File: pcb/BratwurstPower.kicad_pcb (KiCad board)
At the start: 4 copper layers, 85 x 56 mm, 130 parts, among them J1 BarrelJack, J10 GPIO, J2 Raspi, J3 USB1in, J4 USB1out, J5 I2C, J6 I2C, J7 USB2in, J8 USB2out, J9 EXT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

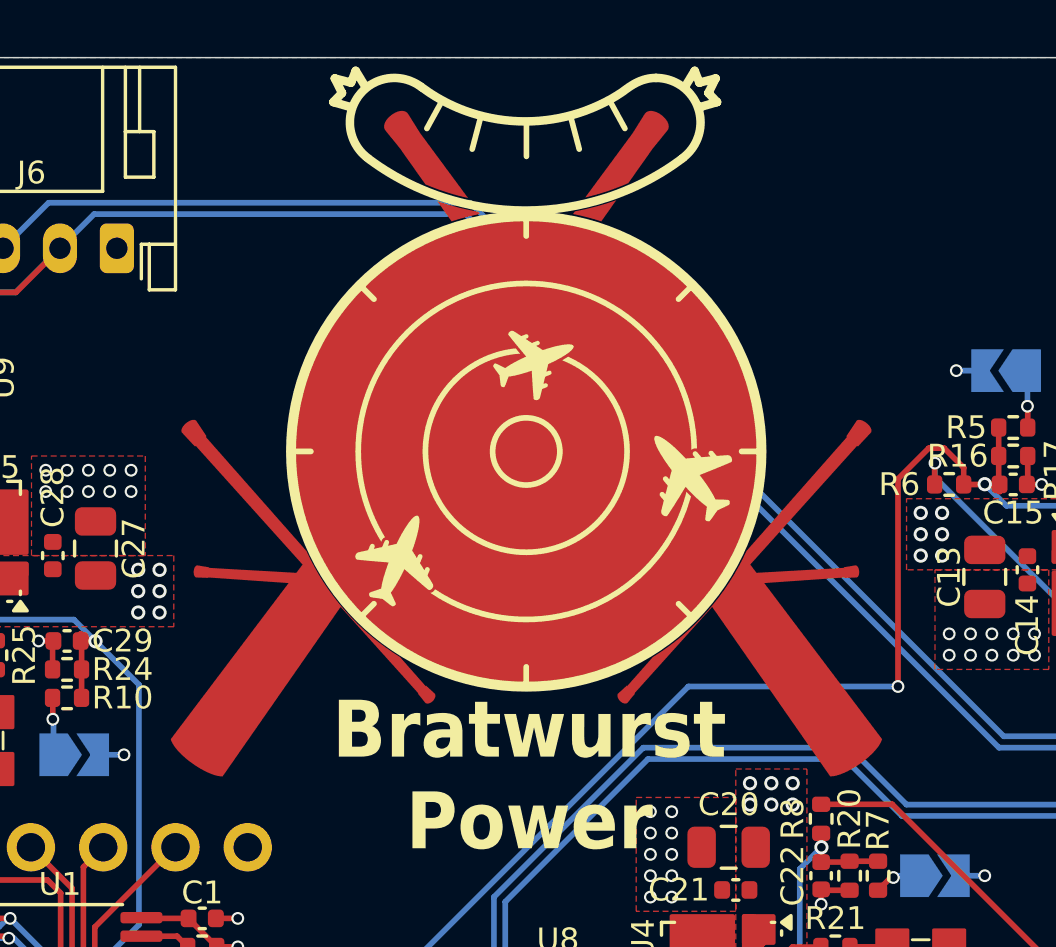
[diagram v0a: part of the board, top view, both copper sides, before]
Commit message: fix: update Bratwurst Logo
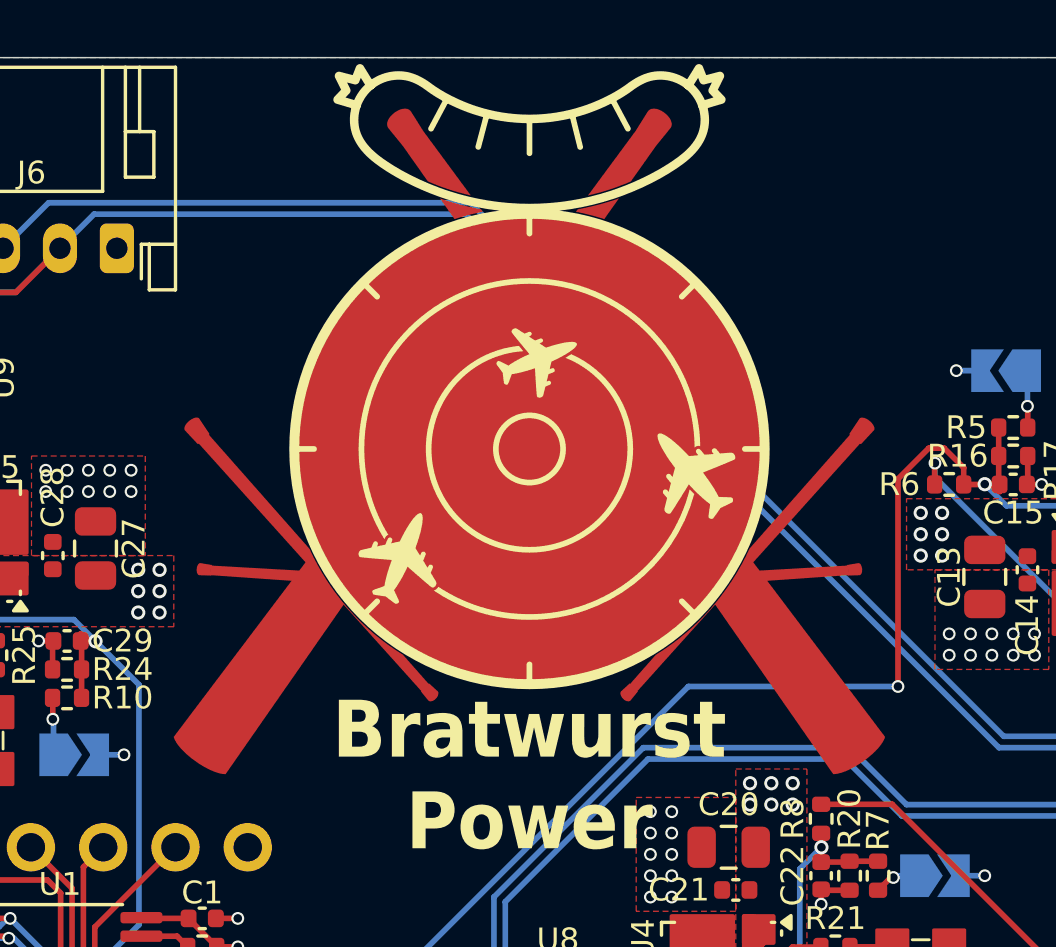
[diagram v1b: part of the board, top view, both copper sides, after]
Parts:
- removed the REF** at (168.2, 92.8)
- added REF**: BratwurstLogo_Filled, BratwurstPower:BratwurstLogo_Filled, F.Cu at (168.2, 93.8)

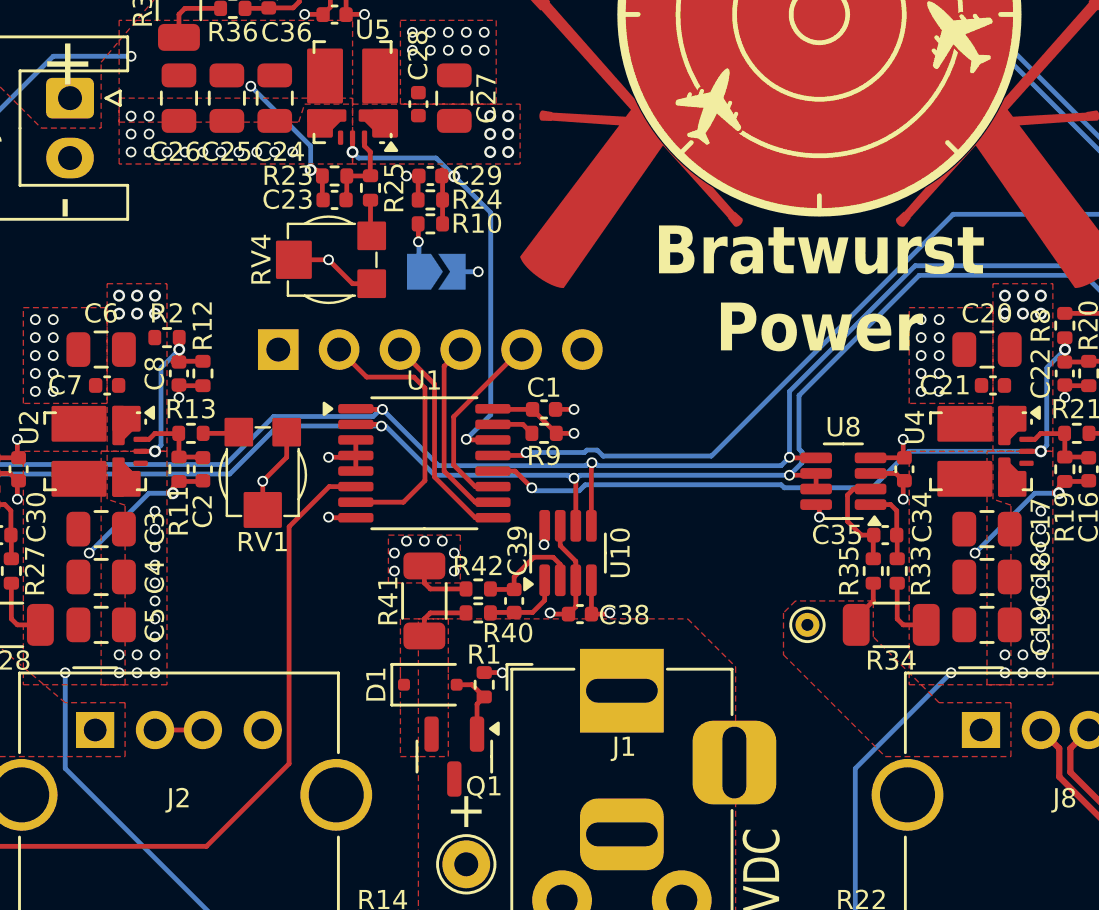
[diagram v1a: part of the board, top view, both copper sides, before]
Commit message: feat: add optional input cap
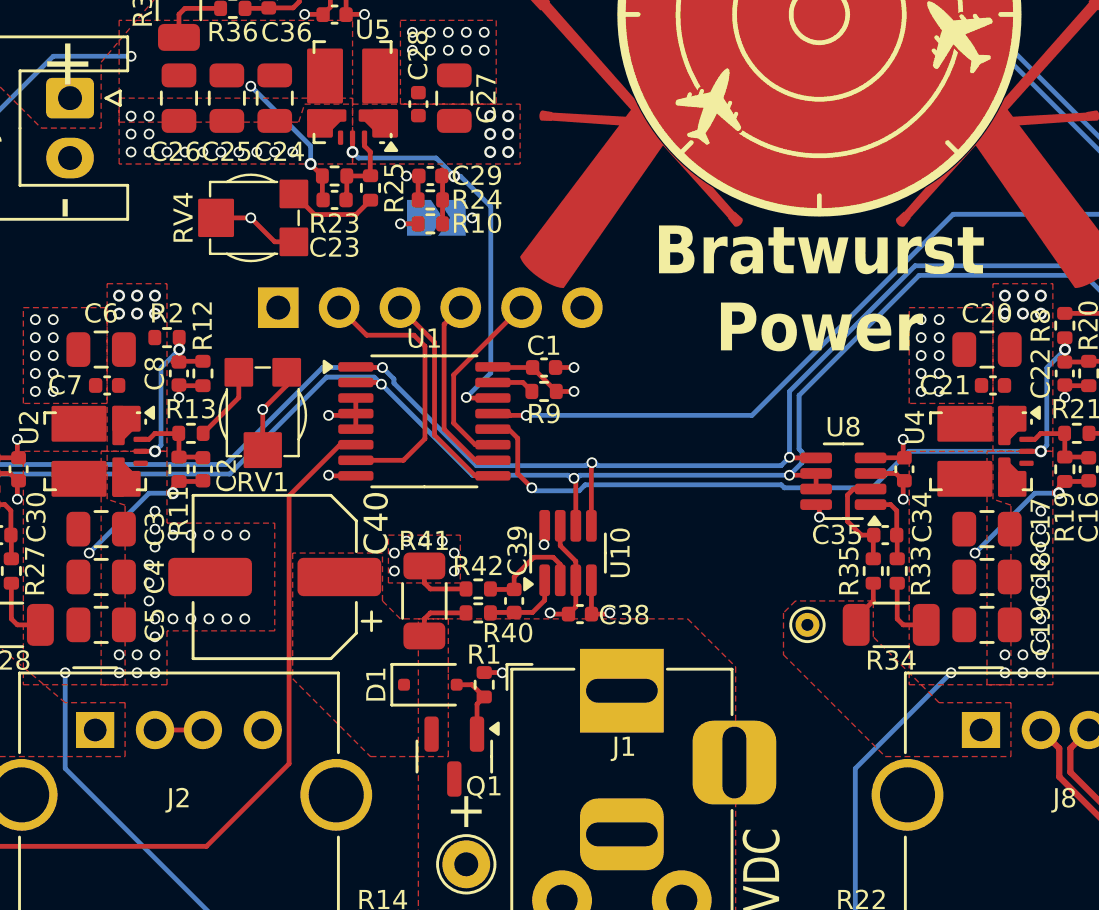
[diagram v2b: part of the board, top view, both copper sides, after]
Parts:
- added C40: 100uF, Capacitor_SMD:CP_Elec_6.3x5.8, F.Cu at (145.5, 117.2)
- moved RV4 3.69 mm to (144.5, 102.2)
- moved RV1 2.50 mm to (145.0, 110.5)
- moved JP3 2.25 mm to (152.2, 102.2)
- moved C1 1.75 mm to (156.8, 108.5)
- moved J10 1.75 mm to (145.7, 106.0)
- moved R9 1.75 mm to (156.8, 109.5)
- moved U1 1.75 mm to (151.8, 110.8)
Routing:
- net /BuckEXT/FBt: track 1.51 -> 3.88 mm
- net SDA: track 140.3 -> 142.0 mm
- net /BuckRaspi/FBt: track 1.51 -> 3.17 mm
- net /Een: track 21.1 -> 19.5 mm
- net /U2en: track 32.3 -> 33.9 mm
- net SCL: track 140.7 -> 142.3 mm
- net /~{BLen}: track 29.4 -> 30.9 mm
- net /U1en: track 50.6 -> 49.7 mm
- net GND: vias 120 -> 130

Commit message: chore: one shall save before committing
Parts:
- C40: footprint Capacitor_SMD:CP_Elec_6.3x5.8 -> Capacitor_THT:CP_Radial_D6.3mm_P2.50mm
- moved C40 1.75 mm to (147.2, 117.2)
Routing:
- net GND: vias 130 -> 120

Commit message: fix: I2C pull-up strength
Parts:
- R3, R4: value 3k3 -> 2k2
- moved JP2 11.9 mm to (180.5, 120.5), turned to 180 degrees
- moved JP1 9.66 mm to (194.5, 92.8), turned to 0 degrees
- moved J10 3.75 mm to (149.4, 106.0)
- moved JP3 2.38 mm to (149.9, 101.9), turned to -90 degrees
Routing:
- net SCL: track 142.3 -> 108.3 mm, vias 5 -> 7
- net SDA: track 142.0 -> 112.6 mm, vias 5 -> 7
- net /5Vu2EN: track 1.49 -> 12.5 mm
- net /5Vu1EN: track 2.01 -> 8.99 mm
- net /IO4: track 8.00 -> 11.9 mm
- net /IO3: track 7.94 -> 10.6 mm
- net /IO1: track 11.4 -> 8.80 mm
- net /Een: track 19.5 -> 18.6 mm
- net /5VeEN: track 1.62 -> 2.35 mm

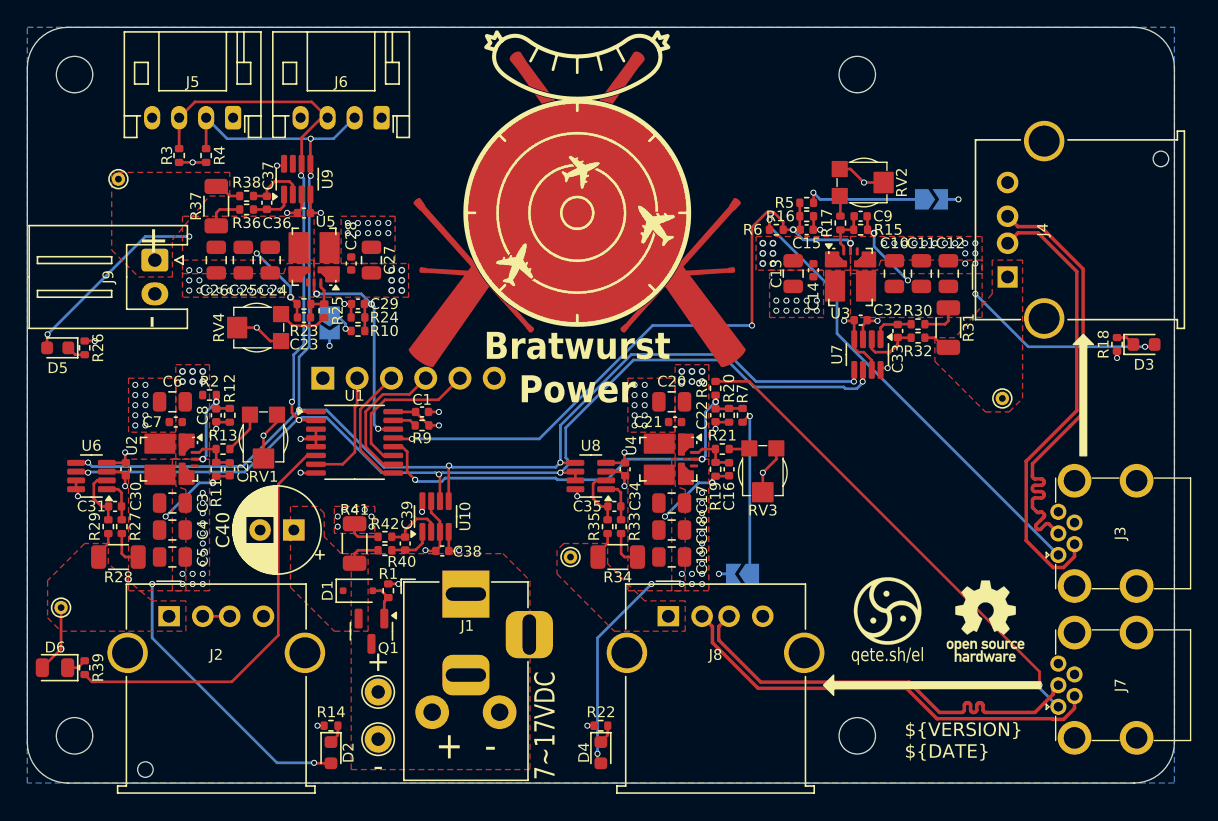
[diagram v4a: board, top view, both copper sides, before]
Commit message: feat: polarity protection for I2C bus
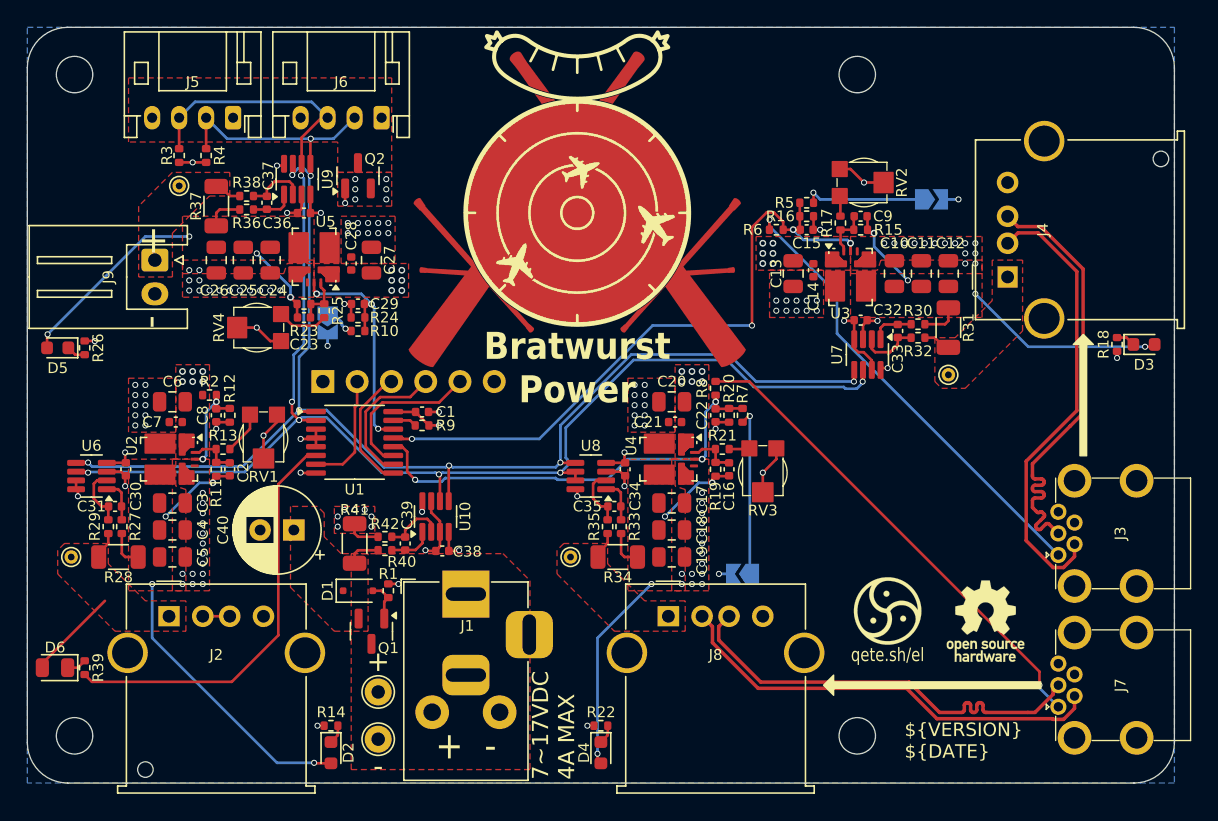
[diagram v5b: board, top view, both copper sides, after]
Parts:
- added Q2: AO3401A, Package_TO_SOT_SMD:SOT-23, F.Cu at (152.0, 91.0)
- moved TP4 4.53 mm to (138.8, 91.8)
- moved TP2 4.37 mm to (195.8, 105.8)
- moved TP1 3.82 mm to (130.8, 119.2)
- moved J10 0.25 mm to (149.4, 106.2)
- moved JP3 0.15 mm to (149.8, 101.9)
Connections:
- J5 pad 4: +3V3 -> /+3V3in
- J6 pad 4: +3V3 -> /+3V3in
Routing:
- net SCL: track 108.3 -> 111.0 mm, vias 7 -> 8
- net /+5Vr: track 7.06 -> 8.91 mm
- net GND: track 42.6 -> 43.7 mm, vias 120 -> 121
- net +3V3: vias 9 -> 15
- added copper zone on F.Cu, net +3V3
- added copper zone on F.Cu, net /+3V3in
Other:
- board text added: "7~17VDC 4A MAX"
- board text removed: "7~17VDC"

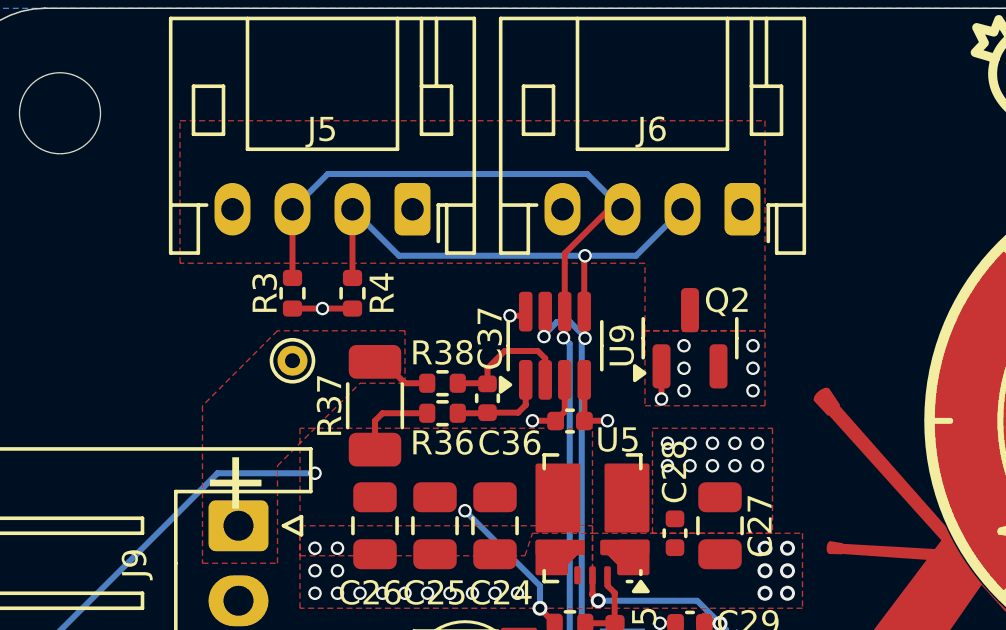
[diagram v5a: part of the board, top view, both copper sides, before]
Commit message: fix: add capacitor to 3V3 rail
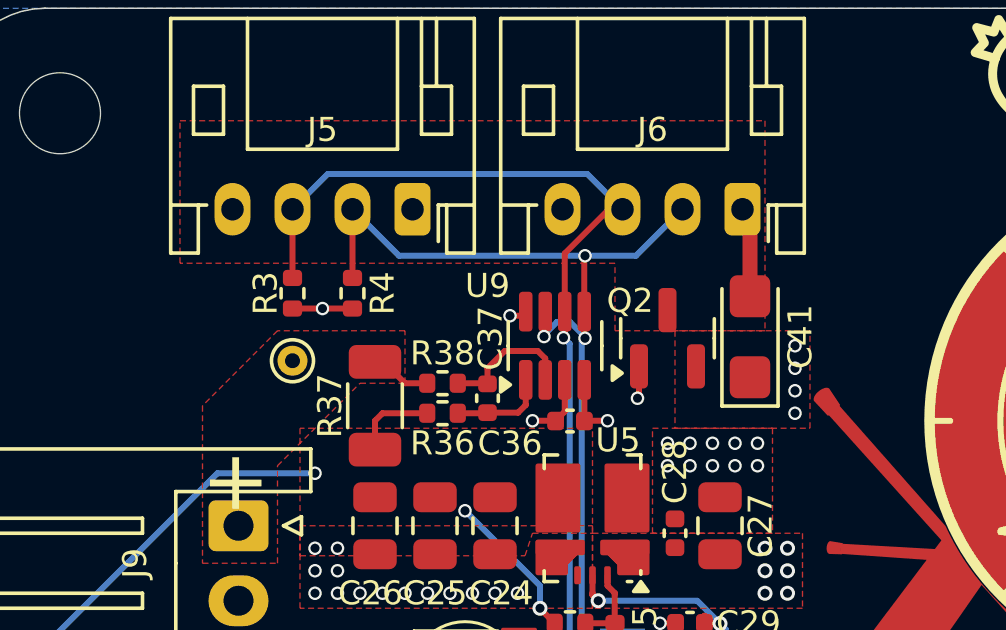
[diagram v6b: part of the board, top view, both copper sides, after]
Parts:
- added C41: 10u, Capacitor_Tantalum_SMD:CP_EIA-3216-18_Kemet-A, F.Cu at (154.0, 91.0)
- moved Q2 0.75 mm to (151.2, 91.0)
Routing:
- net GND: track 43.7 -> 46.7 mm
- net +3V3: vias 15 -> 13

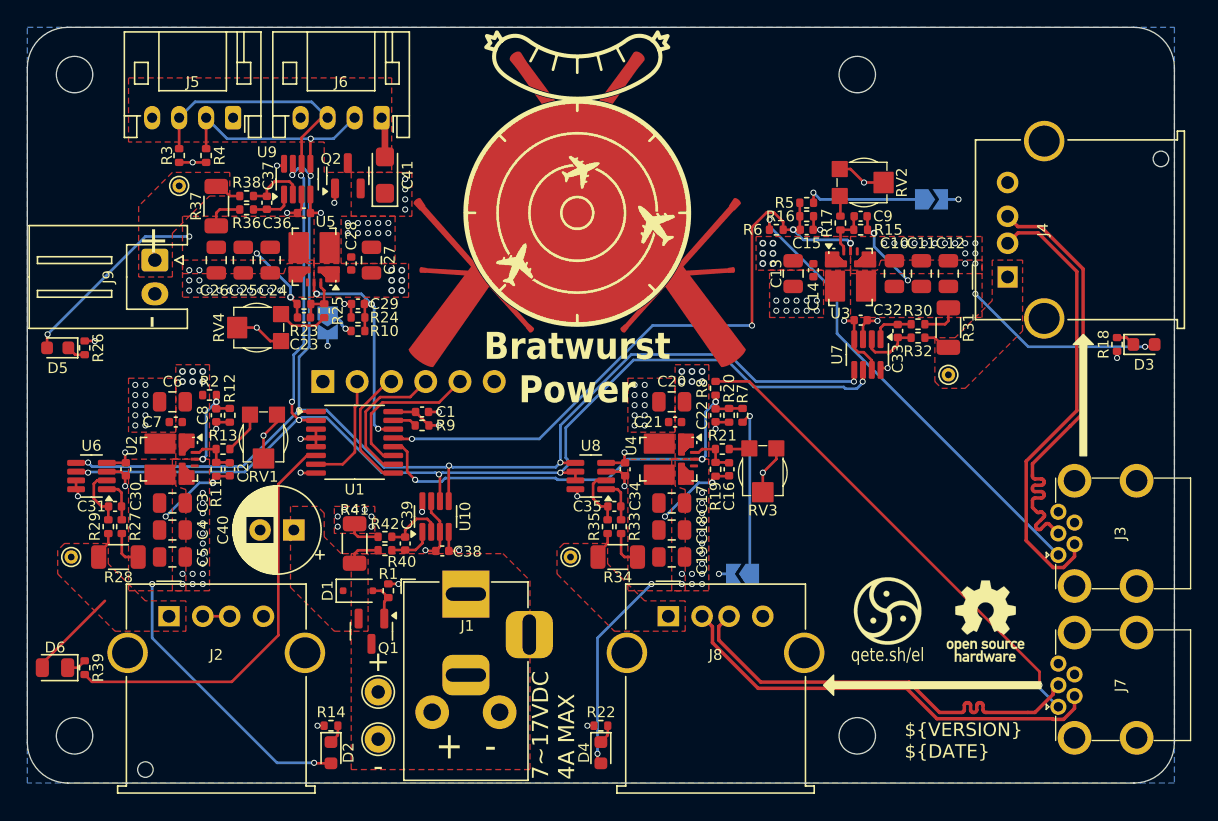
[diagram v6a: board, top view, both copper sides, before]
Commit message: fix: add GND plane on top layer
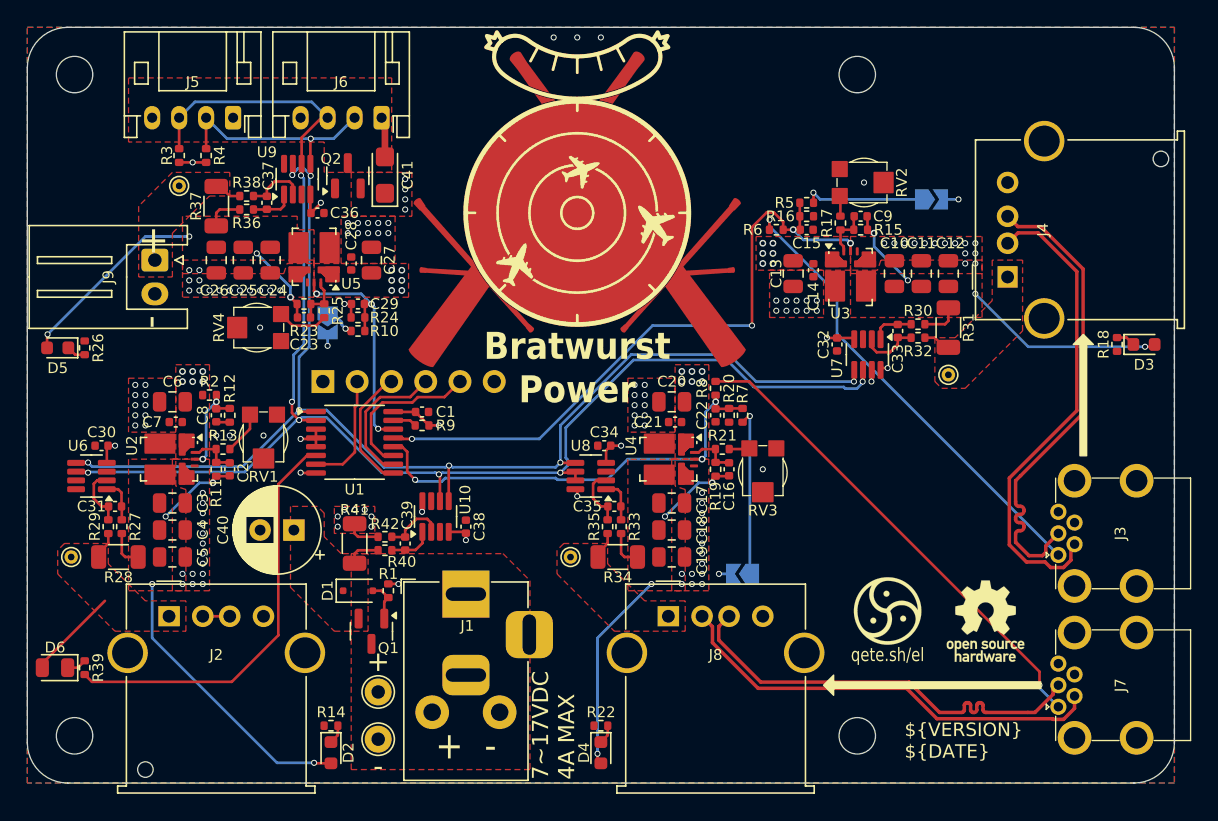
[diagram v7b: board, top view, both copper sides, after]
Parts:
- moved C30 2.51 mm to (133.0, 111.0), turned to 0 degrees
- moved C32 2.51 mm to (187.5, 103.5), turned to 90 degrees
- moved C38 2.51 mm to (160.0, 117.0), turned to -90 degrees
- moved C34 2.34 mm to (170.2, 111.0), turned to 0 degrees
- moved C36 1.00 mm to (149.0, 93.8), turned to 180 degrees
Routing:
- net GND: track 46.7 -> 8.70 mm, vias 121 -> 110
- net +3V3: track 22.9 -> 20.3 mm, vias 13 -> 14
- net /Du1-: track 33.8 -> 35.7 mm
- net /Du1+: track 33.7 -> 35.6 mm
